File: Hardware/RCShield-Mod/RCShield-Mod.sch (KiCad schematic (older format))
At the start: 12 parts, among them K1 PPM_OUT, P1 ANALOG_EXT, P2 DIGI_EXT, P7 Vinput

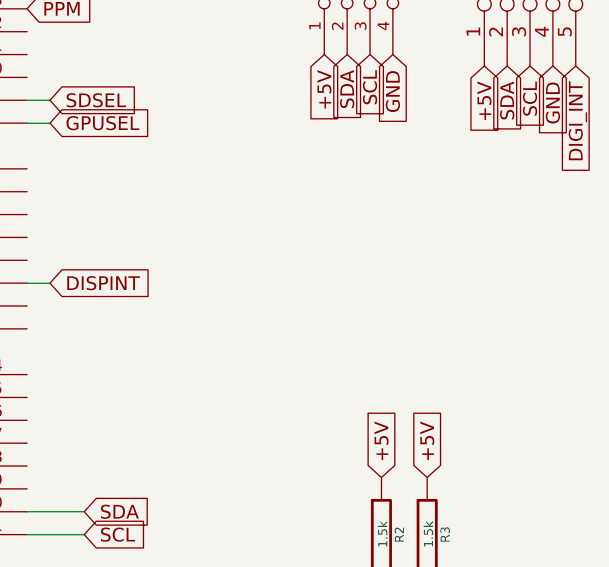
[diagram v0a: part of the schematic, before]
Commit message: Adding Filter Cap to main board Adding ADC Channel re-map Disabling digital IO Configuration in preparation for the new breakout board.
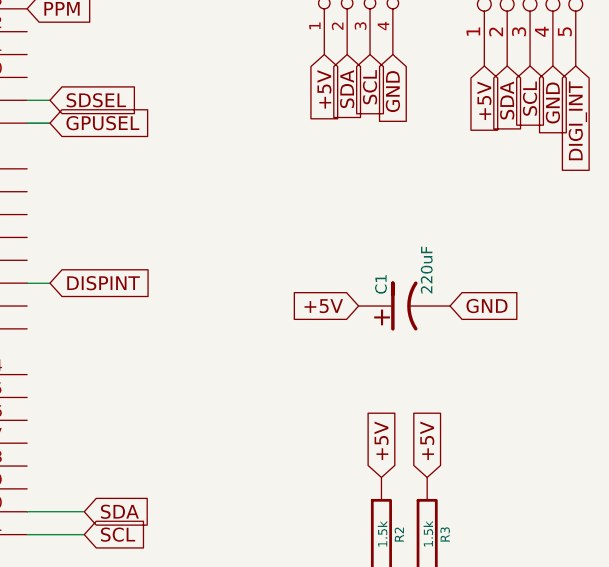
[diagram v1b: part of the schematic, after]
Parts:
- added C1: 220uF, ~, symbol CP1
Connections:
- net +5V: now also C1.1
- net GND: now also C1.2
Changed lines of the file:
@@
 LIBS:valves
 LIBS:arduino_shieldsNCL
+LIBS:RCShield-Mod-cache
 EELAYER 27 0
 EELAYER END
@@
 Sheet 1 1
 Title ""
-Date "12 may 2014"
+Date "18 may 2014"
 Rev ""
 Comp ""
@@
 	0    1    1    0
 $EndComp
+$Comp
+L CP1 C1
+U 1 1 5378EA9A
+P 7500 2750
+F 0 "C1" H 7550 2850 50  0000 L CNN
+F 1 "220uF" H 7550 2650 50  0000 L CNN
+F 2 "~" H 7500 2750 60  0000 C CNN
+F 3 "~" H 7500 2750 60  0000 C CNN
+	1    7500 2750
+	0    -1   -1   0
+$EndComp
+Text GLabel 7300 2750 0    60   Input ~ 0
++5V
+Text GLabel 7700 2750 2    60   Input ~ 0
+GND
 $EndSCHEMATC

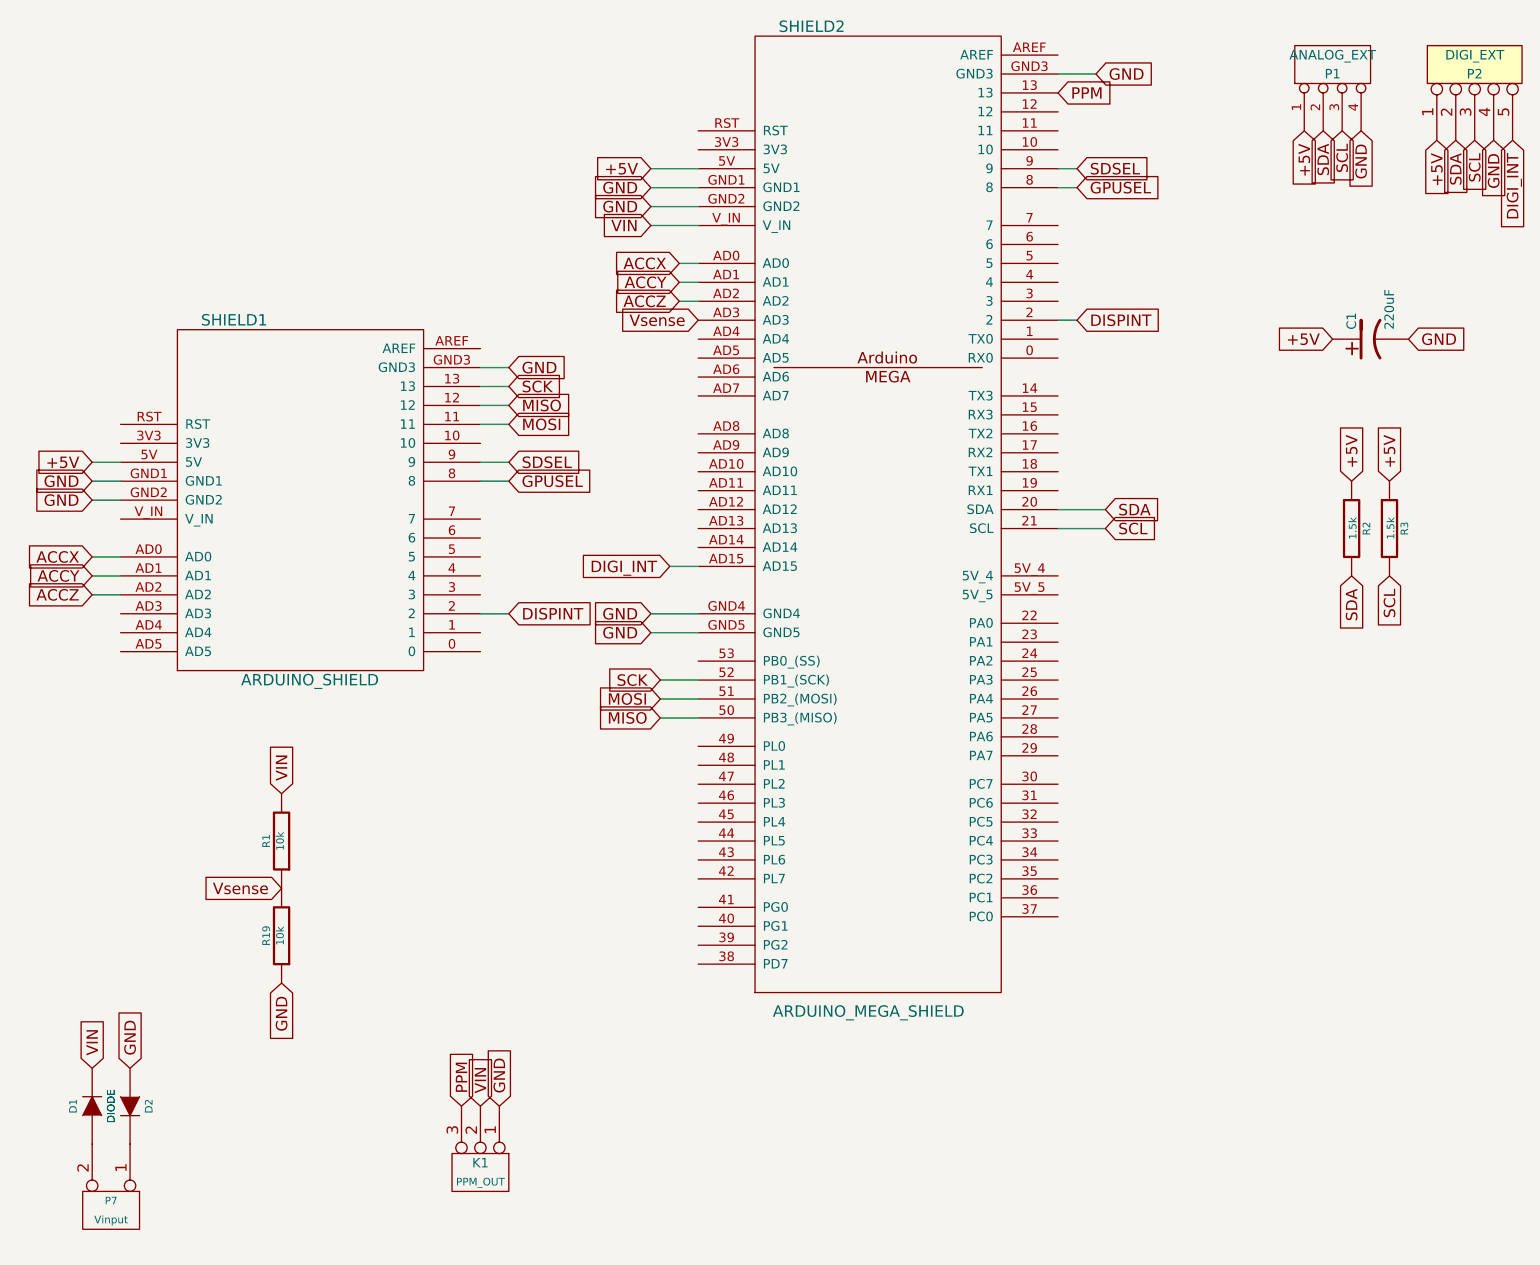
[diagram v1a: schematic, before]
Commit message: * Updating PCB to more rectangular + Caps + On/Off Switch * Disabling Digital Breakout board for now
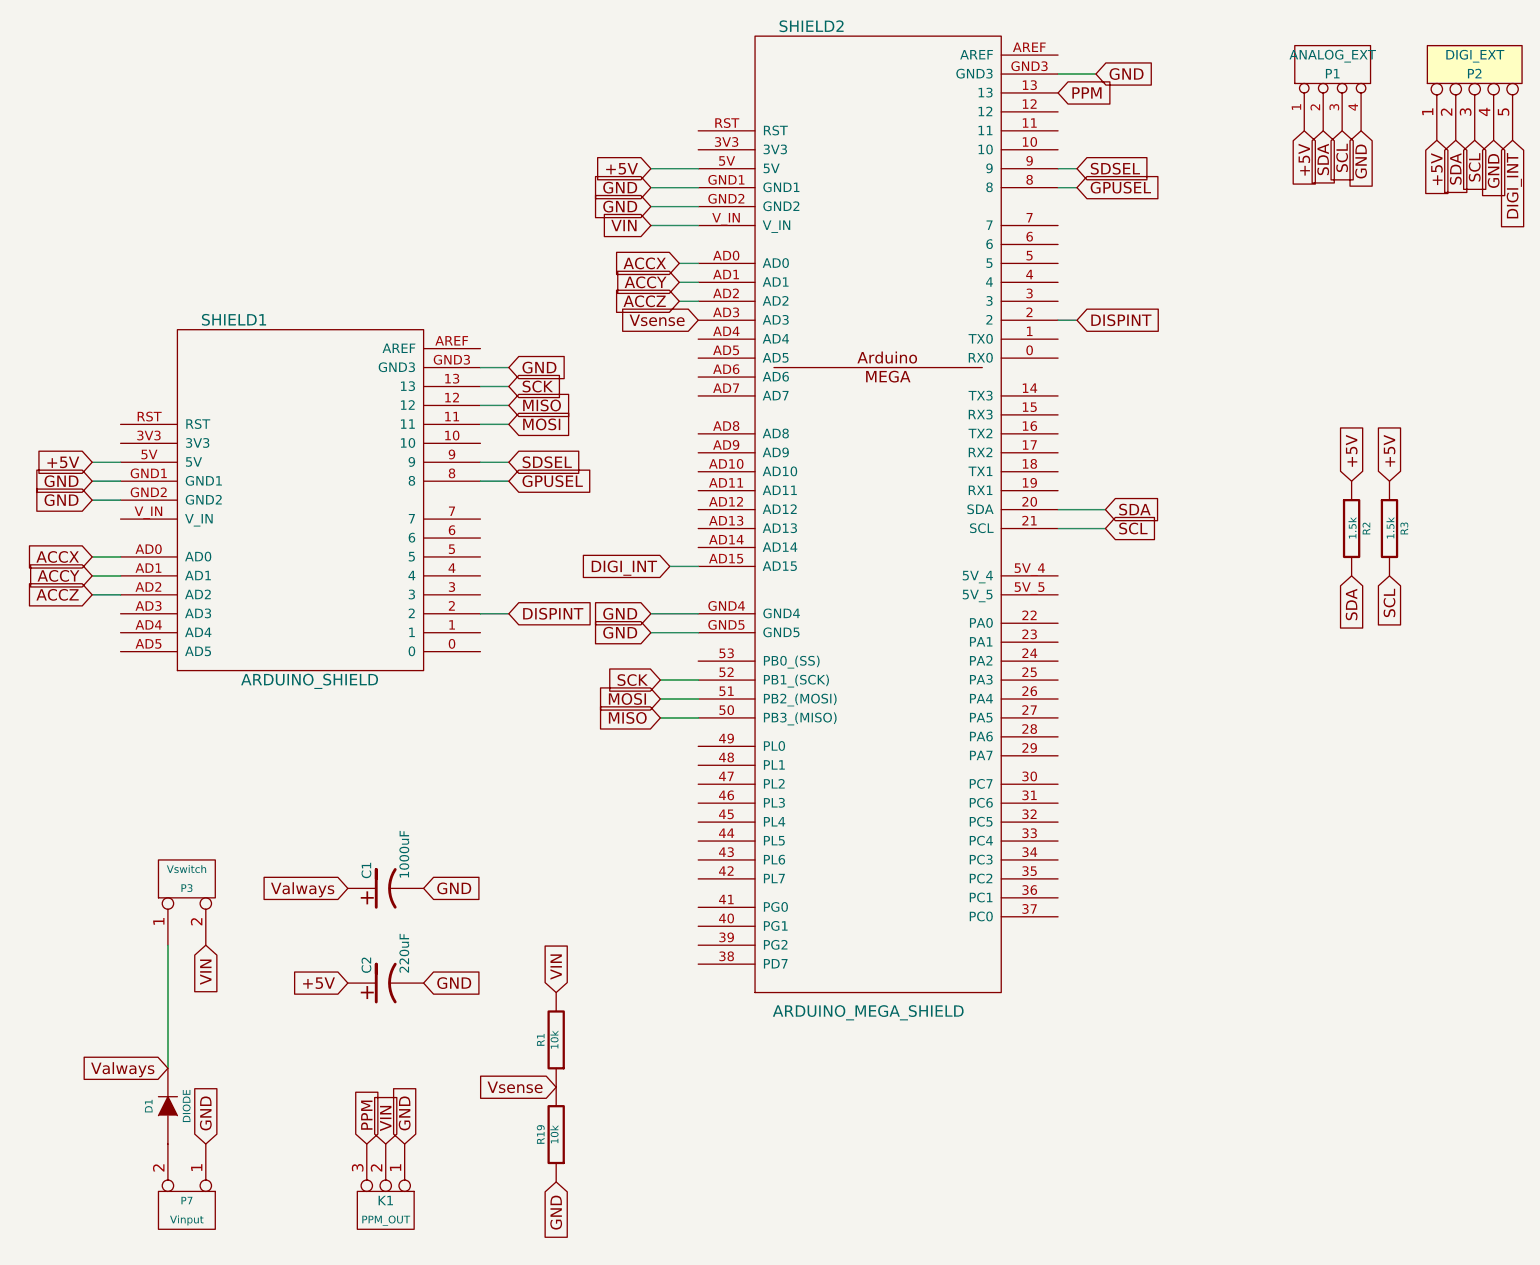
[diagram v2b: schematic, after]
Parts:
- removed D2: DIODE, ~, symbol DIODE
- added C2: 220uF, ~, symbol CP1
- added P3: Vswitch, symbol CONN_2
- C1: value 220uF -> 1000uF
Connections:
- net +5V: now also C2.1; no longer C1.1
- net GND: now also P7.1 (P1), C2.2
- net VIN: now also P3.2 (PM); no longer D1.2 (K)
- new net Valways: C1.1, D1.2 (K), P3.1 (P1)
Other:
- moved on the sheet: C1, D1, K1, P7, R1, R19
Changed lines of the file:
@@
 Sheet 1 1
 Title ""
-Date "18 may 2014"
+Date "8 jun 2014"
 Rev ""
 Comp ""
@@
 L CONN_3 K1
 U 1 1 536F292E
-P 2800 7150
-F 0 "K1" V 2750 7150 50  0000 C CNN
-F 1 "PPM_OUT" V 2850 7150 40  0000 C CNN
-F 2 "" H 2800 7150 60  0000 C CNN
-F 3 "" H 2800 7150 60  0000 C CNN
-	1    2800 7150
+P 2300 7350
+F 0 "K1" V 2250 7350 50  0000 C CNN
+F 1 "PPM_OUT" V 2350 7350 40  0000 C CNN
+F 2 "" H 2300 7350 60  0000 C CNN
+F 3 "" H 2300 7350 60  0000 C CNN
+	1    2300 7350
 	0    1    1    0
 $EndComp
-Text GLabel 2700 6800 1    60   Input ~ 0
+Text GLabel 2200 7000 1    60   Input ~ 0
 PPM
-Text GLabel 2800 6800 1    60   Input ~ 0
+Text GLabel 2300 7000 1    60   Input ~ 0
 VIN
-Text GLabel 2900 6800 1    60   Input ~ 0
+Text GLabel 2400 7000 1    60   Input ~ 0
 GND
 Text GLabel 5850 1450 2    60   Input ~ 0
@@
 L CONN_2 P7
 U 1 1 536F2B46
-P 850 7350
-F 0 "P7" V 800 7350 40  0000 C CNN
-F 1 "Vinput" V 900 7350 40  0000 C CNN
-F 2 "" H 850 7350 60  0000 C CNN
-F 3 "" H 850 7350 60  0000 C CNN
-	1    850  7350
+P 1250 7350
+F 0 "P7" V 1200 7350 40  0000 C CNN
+F 1 "Vinput" V 1300 7350 40  0000 C CNN
+F 2 "" H 1250 7350 60  0000 C CNN
+F 3 "" H 1250 7350 60  0000 C CNN
+	1    1250 7350
 	0    1    1    0
 $EndComp
-Text GLabel 950  6600 1    60   Input ~ 0
-GND
-Text GLabel 750  6600 1    60   Input ~ 0
+Text GLabel 1350 7000 1    60   Input ~ 0
+GND
+Text GLabel 1350 5950 3    60   Input ~ 0
 VIN
 Text GLabel 3950 2650 0    60   Input ~ 0
@@
 L R R1
 U 1 1 536F2BA6
-P 1750 5400
-F 0 "R1" V 1830 5400 40  0000 C CNN
-F 1 "10k" V 1757 5401 40  0000 C CNN
-F 2 "~" V 1680 5400 30  0000 C CNN
-F 3 "~" H 1750 5400 30  0000 C CNN
-	1    1750 5400
+P 3200 6450
+F 0 "R1" V 3280 6450 40  0000 C CNN
+F 1 "10k" V 3207 6451 40  0000 C CNN
+F 2 "~" V 3130 6450 30  0000 C CNN
+F 3 "~" H 3200 6450 30  0000 C CNN
+	1    3200 6450
 	-1   0    0    1
 $EndComp
@@
 L R R19
 U 1 1 536F2BAD
-P 1750 5900
-F 0 "R19" V 1830 5900 40  0000 C CNN
-F 1 "10k" V 1757 5901 40  0000 C CNN
-F 2 "~" V 1680 5900 30  0000 C CNN
-F 3 "~" H 1750 5900 30  0000 C CNN
-	1    1750 5900
+P 3200 6950
+F 0 "R19" V 3280 6950 40  0000 C CNN
+F 1 "10k" V 3207 6951 40  0000 C CNN
+F 2 "~" V 3130 6950 30  0000 C CNN
+F 3 "~" H 3200 6950 30  0000 C CNN
+	1    3200 6950
 	-1   0    0    1
 $EndComp
-Text GLabel 1750 5650 0    60   Input ~ 0
+Text GLabel 3200 6700 0    60   Input ~ 0
 Vsense
-Text GLabel 1750 6150 3    60   Input ~ 0
-GND
-Text GLabel 1750 5150 1    60   Input ~ 0
+Text GLabel 3200 7200 3    60   Input ~ 0
+GND
+Text GLabel 3200 6200 1    60   Input ~ 0
 VIN
 $Comp
@@
 L DIODE D1
 U 1 1 5371403C
-P 750 6800
-F 0 "D1" H 750 6900 40  0000 C CNN
-F 1 "DIODE" H 750 6700 40  0000 C CNN
-F 2 "~" H 750 6800 60  0000 C CNN
-F 3 "~" H 750 6800 60  0000 C CNN
-	1    750  6800
-	0    -1   -1   0
-$EndComp
-$Comp
-L DIODE D2
-U 1 1 53714072
-P 950 6800
-F 0 "D2" H 950 6900 40  0000 C CNN
-F 1 "DIODE" H 950 6700 40  0000 C CNN
-F 2 "~" H 950 6800 60  0000 C CNN
-F 3 "~" H 950 6800 60  0000 C CNN
-	1    950  6800
-	0    1    1    0
+P 1150 6800
+F 0 "D1" H 1150 6900 40  0000 C CNN
+F 1 "DIODE" H 1150 6700 40  0000 C CNN
+F 2 "~" H 1150 6800 60  0000 C CNN
+F 3 "~" H 1150 6800 60  0000 C CNN
+	1    1150 6800
+	0    -1   -1   0
 $EndComp
 $Comp
 L CP1 C1
 U 1 1 5378EA9A
-P 7500 2750
-F 0 "C1" H 7550 2850 50  0000 L CNN
-F 1 "220uF" H 7550 2650 50  0000 L CNN
-F 2 "~" H 7500 2750 60  0000 C CNN
-F 3 "~" H 7500 2750 60  0000 C CNN
-	1    7500 2750
-	0    -1   -1   0
-$EndComp
-Text GLabel 7300 2750 0    60   Input ~ 0
-+5V
-Text GLabel 7700 2750 2    60   Input ~ 0
-GND
+P 2300 5650
+F 0 "C1" H 2350 5750 50  0000 L CNN
+F 1 "1000uF" H 2350 5550 50  0000 L CNN
+F 2 "~" H 2300 5650 60  0000 C CNN
+F 3 "~" H 2300 5650 60  0000 C CNN
+	1    2300 5650
+	0    -1   -1   0
+$EndComp
+Text GLabel 2100 5650 0    60   Input ~ 0
+Valways
+Text GLabel 2500 5650 2    60   Input ~ 0
+GND
+$Comp
+L CONN_2 P3
+U 1 1 5394A61C
+P 1250 5600
+F 0 "P3" V 1200 5600 40  0000 C CNN
+F 1 "Vswitch" V 1300 5600 40  0000 C CNN
+F 2 "" H 1250 5600 60  0000 C CNN
+F 3 "" H 1250 5600 60  0000 C CNN
+	1    1250 5600
+	0    -1   -1   0
+$EndComp
+Wire Wire Line
+	1150 5950 1150 6600
+Text GLabel 1150 6600 0    60   Input ~ 0
+Valways
+$Comp
+L CP1 C2
+U 1 1 5394ABBB
+P 2300 6150
+F 0 "C2" H 2350 6250 50  0000 L CNN
+F 1 "220uF" H 2350 6050 50  0000 L CNN
+F 2 "~" H 2300 6150 60  0000 C CNN
+F 3 "~" H 2300 6150 60  0000 C CNN
+	1    2300 6150
+	0    -1   -1   0
+$EndComp
+Text GLabel 2500 6150 2    60   Input ~ 0
+GND
+Text GLabel 2100 6150 0    60   Input ~ 0
++5V
 $EndSCHEMATC
